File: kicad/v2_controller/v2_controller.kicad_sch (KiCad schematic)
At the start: 0 parts

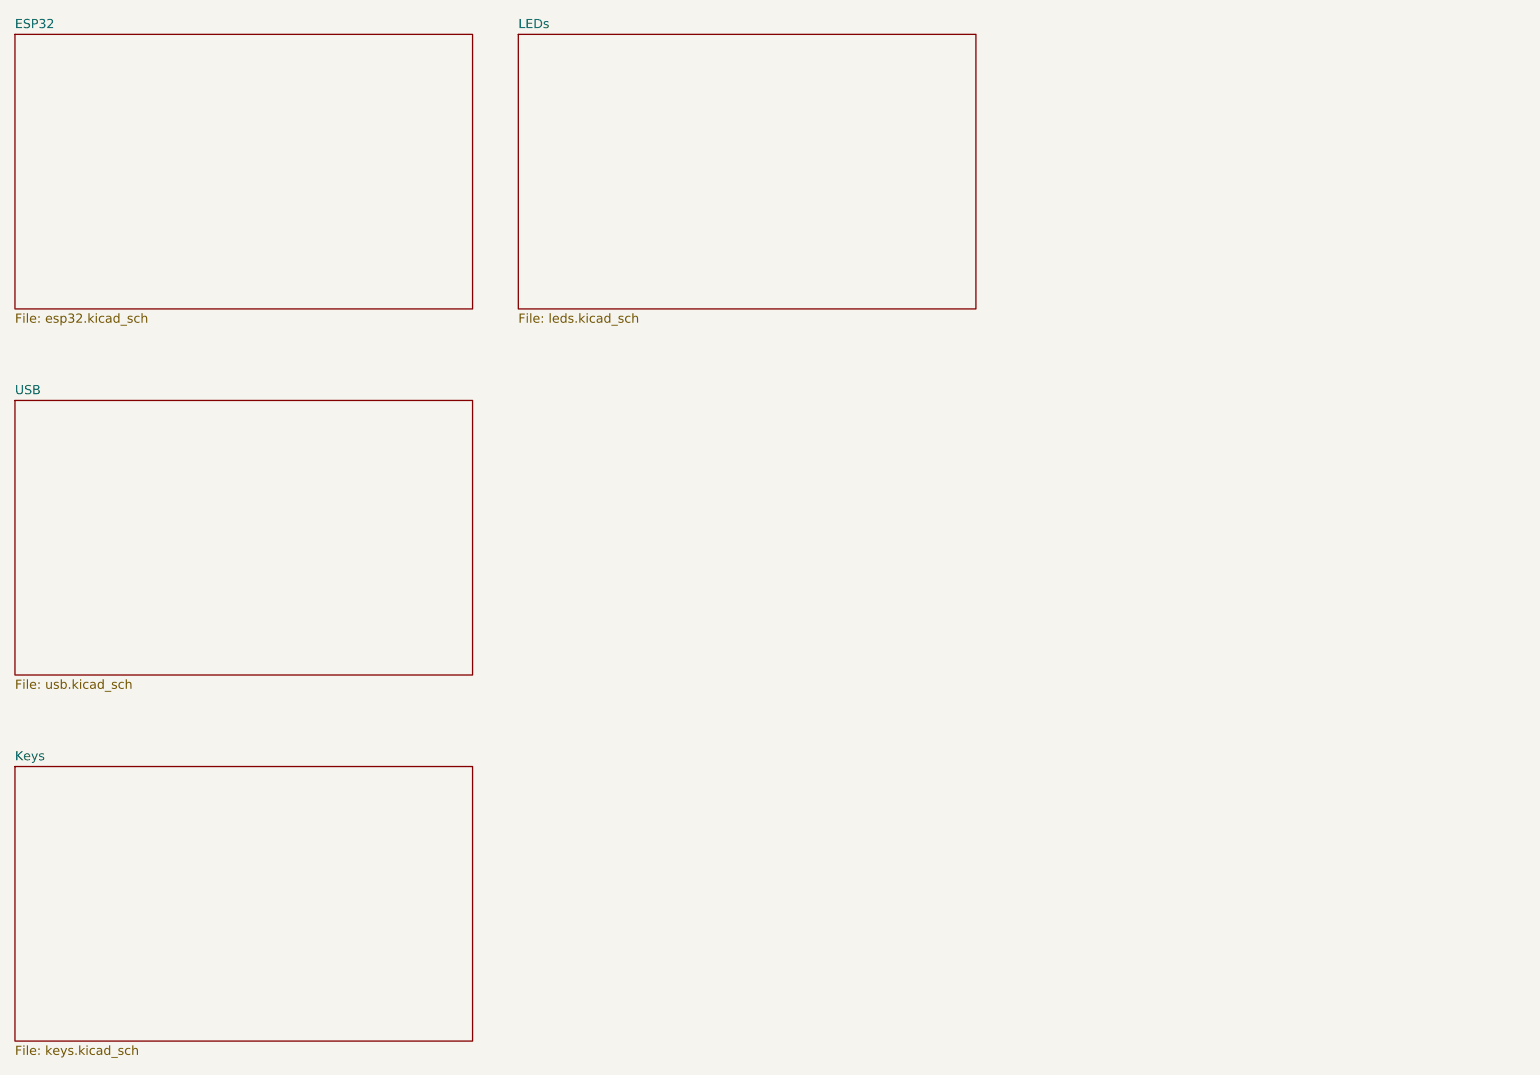
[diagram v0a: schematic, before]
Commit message: [kicad] update v2 controller to use hierarchical labels
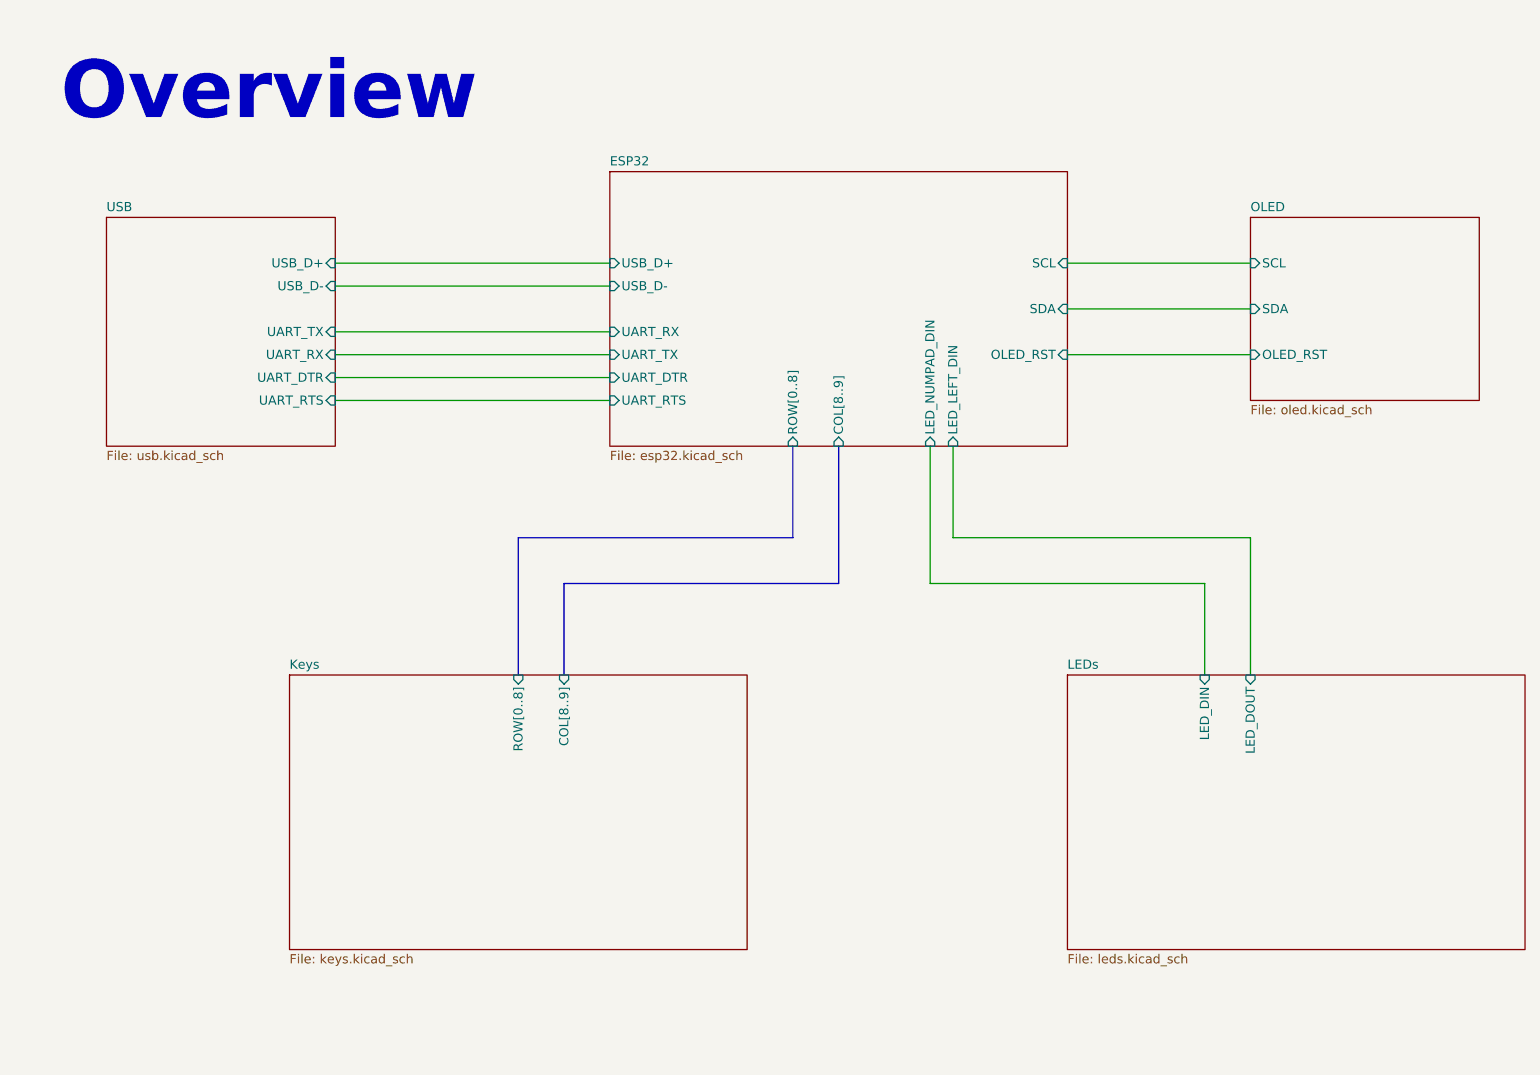
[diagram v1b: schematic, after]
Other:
- added sheet OLED (oled.kicad_sch)
- sheet ESP32 ports: added COL[8..9], LED_LEFT_DIN, LED_NUMPAD_DIN, OLED_RST, ROW[0..8], SCL, SDA, UART_DTR, UART_RTS, UART_RX, UART_TX, USB_D+, USB_D-; removed none
- sheet Keys ports: added COL[8..9], ROW[0..8]; removed none
- sheet LEDs ports: added LED_DIN, LED_DOUT; removed none
- sheet USB ports: added UART_DTR, UART_RTS, UART_RX, UART_TX, USB_D+, USB_D-; removed none
- note added: "Overview"
- title: (none) -> Overview
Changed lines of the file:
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@@
 (kicad_sch (version 20230121) (generator eeschema)
   (paper "A4")
-  (sheet (at 25.4 69.85) (size 63.5 38.1) (fields_autoplaced)
-    (stroke (width 0.1524) (type solid))
-    (fill (color 0 0 0 0.0000))
-    (property "Sheetname" "USB" (at 25.4 69.1384 0)
-      (effects (font (size 1.27 1.27)) (justify left bottom))
-    )
-    (property "Sheetfile" "usb.kicad_sch" (at 25.4 108.5346 0)
-      (effects (font (size 1.27 1.27)) (justify left top))
+  (title_block
+    (title "Overview")
+  )
+  (wire (pts (xy 171.45 57.15) (xy 196.85 57.15))
+    (stroke (width 0) (type default))
+  )
+  (wire (pts (xy 69.85 66.675) (xy 107.95 66.675))
+    (stroke (width 0) (type default))
+  )
+  (wire (pts (xy 69.85 63.5) (xy 107.95 63.5))
+    (stroke (width 0) (type default))
+  )
+  (wire (pts (xy 152.4 95.25) (xy 190.5 95.25))
+    (stroke (width 0) (type default))
+  )
+  (wire (pts (xy 155.575 88.9) (xy 196.85 88.9))
+    (stroke (width 0) (type default))
+  )
+  (wire (pts (xy 152.4 76.2) (xy 152.4 95.25))
+    (stroke (width 0) (type default))
+  )
+  (wire (pts (xy 171.45 50.8) (xy 196.85 50.8))
+    (stroke (width 0) (type default))
+  )
+  (wire (pts (xy 69.85 50.8) (xy 107.95 50.8))
+    (stroke (width 0) (type default))
+  )
+  (wire (pts (xy 155.575 76.2) (xy 155.575 88.9))
+    (stroke (width 0) (type default))
+  )
+  (wire (pts (xy 69.85 53.975) (xy 107.95 53.975))
+    (stroke (width 0) (type default))
+  )
+  (bus (pts (xy 133.35 88.9) (xy 95.25 88.9))
+    (stroke (width 0) (type default))
+  )
+  (wire (pts (xy 171.45 63.5) (xy 196.85 63.5))
+    (stroke (width 0) (type default))
+  )
+  (wire (pts (xy 190.5 95.25) (xy 190.5 107.95))
+    (stroke (width 0) (type default))
+  )
+  (wire (pts (xy 196.85 88.9) (xy 196.85 107.95))
+    (stroke (width 0) (type default))
+  )
+  (bus (pts (xy 139.7 95.25) (xy 101.6 95.25))
+    (stroke (width 0) (type default))
+  )
+  (bus (pts (xy 101.6 95.25) (xy 101.6 107.95))
+    (stroke (width 0) (type default))
+  )
+  (bus (pts (xy 95.25 88.9) (xy 95.25 107.95))
+    (stroke (width 0) (type default))
+  )
+  (bus (pts (xy 139.7 76.2) (xy 139.7 95.25))
+    (stroke (width 0) (type default))
+  )
+  (bus (pts (xy 133.35 76.2) (xy 133.35 88.9))
+    (stroke (width 0) (type default))
+  )
+  (wire (pts (xy 69.85 69.85) (xy 107.95 69.85))
+    (stroke (width 0) (type default))
+  )
+  (wire (pts (xy 69.85 60.325) (xy 107.95 60.325))
+    (stroke (width 0) (type default))
+  )
+  (text "Overview" (at 31.75 31.75 0)
+    (effects (font (size 8 8) (thickness 1) bold (color 194 0 0 1)) (justify left bottom))
+  )
+  (sheet (at 38.1 44.45) (size 31.75 31.75) (fields_autoplaced)
+    (stroke (width 0.1524) (type solid))
+    (fill (color 0 0 0 0.0000))
+    (property "Sheetname" "USB" (at 38.1 43.7384 0)
+      (effects (font (size 1.27 1.27)) (justify left bottom))
+    )
+    (property "Sheetfile" "usb.kicad_sch" (at 38.1 76.7846 0)
+      (effects (font (size 1.27 1.27)) (justify left top))
+    )
+    (pin "UART_DTR" input (at 69.85 66.675 0)
+      (effects (font (size 1.27 1.27)) (justify right))
+    )
+    (pin "UART_RTS" input (at 69.85 69.85 0)
+      (effects (font (size 1.27 1.27)) (justify right))
+    )
+    (pin "UART_TX" input (at 69.85 60.325 0)
+      (effects (font (size 1.27 1.27)) (justify right))
+    )
+    (pin "UART_RX" input (at 69.85 63.5 0)
+      (effects (font (size 1.27 1.27)) (justify right))
+    )
+    (pin "USB_D+" input (at 69.85 50.8 0)
+      (effects (font (size 1.27 1.27)) (justify right))
+    )
+    (pin "USB_D-" input (at 69.85 53.975 0)
+      (effects (font (size 1.27 1.27)) (justify right))
     )
     (instances
@@
     )
   )
-  (sheet (at 25.4 120.65) (size 63.5 38.1) (fields_autoplaced)
-    (stroke (width 0.1524) (type solid))
-    (fill (color 0 0 0 0.0000))
-    (property "Sheetname" "Keys" (at 25.4 119.9384 0)
-      (effects (font (size 1.27 1.27)) (justify left bottom))
-    )
-    (property "Sheetfile" "keys.kicad_sch" (at 25.4 159.3346 0)
-      (effects (font (size 1.27 1.27)) (justify left top))
+  (sheet (at 63.5 107.95) (size 63.5 38.1) (fields_autoplaced)
+    (stroke (width 0.1524) (type solid))
+    (fill (color 0 0 0 0.0000))
+    (property "Sheetname" "Keys" (at 63.5 107.2384 0)
+      (effects (font (size 1.27 1.27)) (justify left bottom))
+    )
+    (property "Sheetfile" "keys.kicad_sch" (at 63.5 146.6346 0)
+      (effects (font (size 1.27 1.27)) (justify left top))
+    )
+    (pin "ROW[0..8]" input (at 95.25 107.95 90)
+      (effects (font (size 1.27 1.27)) (justify right))
+    )
+    (pin "COL[8..9]" input (at 101.6 107.95 90)
+      (effects (font (size 1.27 1.27)) (justify right))
     )
     (instances
@@
     )
   )
-  (sheet (at 95.25 19.05) (size 63.5 38.1) (fields_autoplaced)
-    (stroke (width 0.1524) (type solid))
-    (fill (color 0 0 0 0.0000))
-    (property "Sheetname" "LEDs" (at 95.25 18.3384 0)
-      (effects (font (size 1.27 1.27)) (justify left bottom))
-    )
-    (property "Sheetfile" "leds.kicad_sch" (at 95.25 57.7346 0)
-      (effects (font (size 1.27 1.27)) (justify left top))
+  (sheet (at 171.45 107.95) (size 63.5 38.1) (fields_autoplaced)
+    (stroke (width 0.1524) (type solid))
+    (fill (color 0 0 0 0.0000))
+    (property "Sheetname" "LEDs" (at 171.45 107.2384 0)
+      (effects (font (size 1.27 1.27)) (justify left bottom))
+    )
+    (property "Sheetfile" "leds.kicad_sch" (at 171.45 146.6346 0)
+      (effects (font (size 1.27 1.27)) (justify left top))
+    )
+    (pin "LED_DOUT" input (at 196.85 107.95 90)
+      (effects (font (size 1.27 1.27)) (justify right))
+    )
+    (pin "LED_DIN" input (at 190.5 107.95 90)
+      (effects (font (size 1.27 1.27)) (justify right))
     )
     (instances
@@
     )
   )
-  (sheet (at 25.4 19.05) (size 63.5 38.1) (fields_autoplaced)
-    (stroke (width 0.1524) (type solid))
-    (fill (color 0 0 0 0.0000))
-    (property "Sheetname" "ESP32" (at 25.4 18.3384 0)
-      (effects (font (size 1.27 1.27)) (justify left bottom))
-    )
-    (property "Sheetfile" "esp32.kicad_sch" (at 25.4 57.7346 0)
-      (effects (font (size 1.27 1.27)) (justify left top))
+  (sheet (at 107.95 38.1) (size 63.5 38.1) (fields_autoplaced)
+    (stroke (width 0.1524) (type solid))
+    (fill (color 0 0 0 0.0000))
+    (property "Sheetname" "ESP32" (at 107.95 37.3884 0)
+      (effects (font (size 1.27 1.27)) (justify left bottom))
+    )
+    (property "Sheetfile" "esp32.kicad_sch" (at 107.95 76.7846 0)
+      (effects (font (size 1.27 1.27)) (justify left top))
+    )
+    (pin "UART_DTR" input (at 107.95 66.675 180)
+      (effects (font (size 1.27 1.27)) (justify left))
+    )
+    (pin "UART_RTS" input (at 107.95 69.85 180)
+      (effects (font (size 1.27 1.27)) (justify left))
+    )
+    (pin "OLED_RST" input (at 171.45 63.5 0)
+      (effects (font (size 1.27 1.27)) (justify right))
+    )
+    (pin "SCL" input (at 171.45 50.8 0)
+      (effects (font (size 1.27 1.27)) (justify right))
+    )
+    (pin "SDA" input (at 171.45 57.15 0)
+      (effects (font (size 1.27 1.27)) (justify right))
+    )
+    (pin "UART_TX" input (at 107.95 63.5 180)
+      (effects (font (size 1.27 1.27)) (justify left))
+    )
+    (pin "UART_RX" input (at 107.95 60.325 180)
+      (effects (font (size 1.27 1.27)) (justify left))
+    )
+    (pin "USB_D-" input (at 107.95 53.975 180)
+      (effects (font (size 1.27 1.27)) (justify left))
+    )
+    (pin "USB_D+" input (at 107.95 50.8 180)
+      (effects (font (size 1.27 1.27)) (justify left))
+    )
+    (pin "LED_NUMPAD_DIN" input (at 152.4 76.2 270)
+      (effects (font (size 1.27 1.27)) (justify left))
+    )
+    (pin "LED_LEFT_DIN" input (at 155.575 76.2 270)
+      (effects (font (size 1.27 1.27)) (justify left))
+    )
+    (pin "COL[8..9]" input (at 139.7 76.2 270)
+      (effects (font (size 1.27 1.27)) (justify left))
+    )
+    (pin "ROW[0..8]" input (at 133.35 76.2 270)
+      (effects (font (size 1.27 1.27)) (justify left))
     )
     (instances
@@
       )
     )
+  )
+  (sheet (at 196.85 44.45) (size 31.75 25.4) (fields_autoplaced)
+    (stroke (width 0.1524) (type solid))
+    (fill (color 0 0 0 0.0000))
+    (property "Sheetname" "OLED" (at 196.85 43.7384 0)
+      (effects (font (size 1.27 1.27)) (justify left bottom))
+    )
+    (property "Sheetfile" "oled.kicad_sch" (at 196.85 70.4346 0)
+      (effects (font (size 1.27 1.27)) (justify left top))
+    )
+    (pin "OLED_RST" input (at 196.85 63.5 180)
+      (effects (font (size 1.27 1.27)) (justify left))
+    )
+    (pin "SDA" input (at 196.85 57.15 180)
+      (effects (font (size 1.27 1.27)) (justify left))
+    )
+    (pin "SCL" input (at 196.85 50.8 180)
+      (effects (font (size 1.27 1.27)) (justify left))
+    )
+    (instances
+      (project "v2_controller"
+        (path "/102c646f-89e8-474a-be69-05b634400329" (page "6"))
+      )
+    )

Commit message: [kicad] more routing
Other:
- sheet ESP32 ports: added LED_RIGHT_DIN; removed LED_LEFT_DIN
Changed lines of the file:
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@@
       (effects (font (size 1.27 1.27)) (justify left))
     )
-    (pin "LED_LEFT_DIN" input (at 155.575 76.2 270)
+    (pin "LED_RIGHT_DIN" input (at 155.575 76.2 270)
       (effects (font (size 1.27 1.27)) (justify left))
     )
